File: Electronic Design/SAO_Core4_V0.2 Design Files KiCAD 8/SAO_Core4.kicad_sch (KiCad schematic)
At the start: 84 parts, among them Q1 MMBT4403LT1G, Q13 MMBT4403LT1G, Q14 MMBT4401LT1G, Q17 MMBT4403LT1G, Q18 MMBT4401LT1G, Q2 MMBT4401LT1G, Q21 Q_NMOS_DGS_AO3400A, Q22 SL3401A, Q3 MMBT4403LT1G, Q4 MMBT4401LT1G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

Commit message: Clean-up schematic DRC
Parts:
- removed X9: QWIIC, Connector_JST:JST_SH_SM04B-SRSS-TB_1x04-1MP_P1.00mm_Horizontal, symbol ANDY_SYMBOL_LIBRARY:Connector_QWIIC_4x1_MP
- added X3: QWIIC, Connector_JST:JST_SH_SM04B-SRSS-TB_1x04-1MP_P1.00mm_Horizontal, symbol ANDY_SYMBOL_LIBRARY:Connector_QWIIC_4x1_MP_P1.00
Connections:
- net GND: now also X3.1 (Pin_1)
- net SCL: now also X3.4 (Pin_4)
- net SDA: now also X3.3 (Pin_3)
- net at JP21.2 (C): now also X3.2 (Pin_2)
- net VMEM renamed 3V3

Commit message: Begin refinements for HWV0.2.0
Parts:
- removed JP21: V_SEL, Jumper:SolderJumper-3_P1.3mm_Bridged12_Pad1.0x1.5mm, symbol Jumper:SolderJumper_3_Bridged12
- removed JP22: INTA, Jumper:SolderJumper-2_P1.3mm_Open_Pad1.0x1.5mm, symbol Jumper:SolderJumper_2_Open
- removed JP23: INTB, Jumper:SolderJumper-2_P1.3mm_Open_Pad1.0x1.5mm, symbol Jumper:SolderJumper_2_Open
- removed JP24, JP25: CM_SNS_SEL, Jumper:SolderJumper-3_P1.3mm_Bridged12_Pad1.0x1.5mm, symbol Jumper:SolderJumper_3_Bridged12
- removed TP6: GPB6, Andy_Footprint_Library:TestPoint_THTPad_D1.5mm_Drill1.0mm, symbol Connector:TestPoint_Probe
- removed TP7: GPB7, Andy_Footprint_Library:TestPoint_THTPad_D1.5mm_Drill1.0mm, symbol Connector:TestPoint_Probe
- removed X2: SAO_conn_SFH11-NBPC-D03-ST-BK, Andy_Footprint_Library:Badgelife-SAOv169-BADGE-2x3, symbol ANDY_SYMBOL_LIBRARY:SAO_conn_SFH11-NBPC-D03-ST-BK-badgelife_shitty_addon_v169bis
- removed X3: QWIIC, Connector_JST:JST_SH_SM04B-SRSS-TB_1x04-1MP_P1.00mm_Horizontal, symbol ANDY_SYMBOL_LIBRARY:Connector_QWIIC_4x1_MP_P1.00
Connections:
- net GPIO2 is gone; now on net CM_SNS_PLS: X1.6 (GPIO2)
- net SPARE_GPA6 is gone; now on net CM_EN: U11.27 (GPA6)
- net CMDQ-7N9P renamed CMDQ-7N
- net CMDQ-7N: no longer R17.2
- net CMDQ-7P9N renamed CMDQ-7P
- net CMDQ-7P: no longer R18.2
- net SPARE_GPB6 renamed CMDQ-9N
- net CMDQ-9N: now also R18.2
- net SPARE_GPB7 renamed CMDQ-9P
- net CMDQ-9P: now also R17.2
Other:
- note added: "(SAO RX)"
- note added: "(SAO TX)"
- note added: "Learn about I2C GPIO Expanders here: https://learn.adafruit.com/adafruit-mcp23017-i2c-gpio-expander 7 Address bits: 010 0[A2-A1-A0] HEX 0x20 to 0x27 (default 27) DEC 32 to 39 (default 39)"
- note added: "SAO, I2C"
- note added: "Shift LED connections up 2 pins, tying B3/4 to 7N/7P. The order will look cleaner, and LED pixel numbering will match GPB numbers."
- note removed: "Learn about I2C GPIO Expanders here: https://learn.adafruit.com/adafruit-mcp23017-i2c-gpio-expander 7 Address bits: 010 0[A2-A1-A0] HEX 0x: 2 [0 to 7]"
- note removed: "QWIIC I2C"
- note removed: "SAO #2 (OUT/TOP)"
- note removed: "SAO, QWIIC, STEMMA QT, I2C"

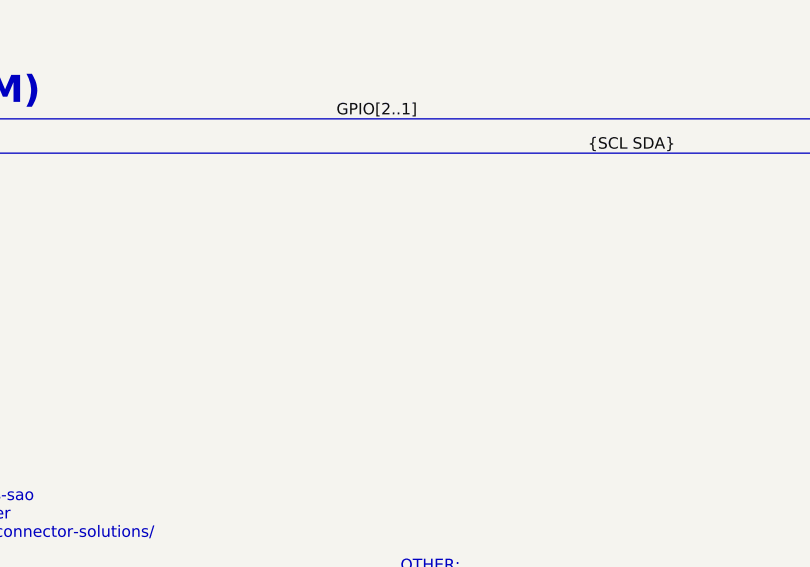
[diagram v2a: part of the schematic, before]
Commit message: Shrink V0.2 PCB size
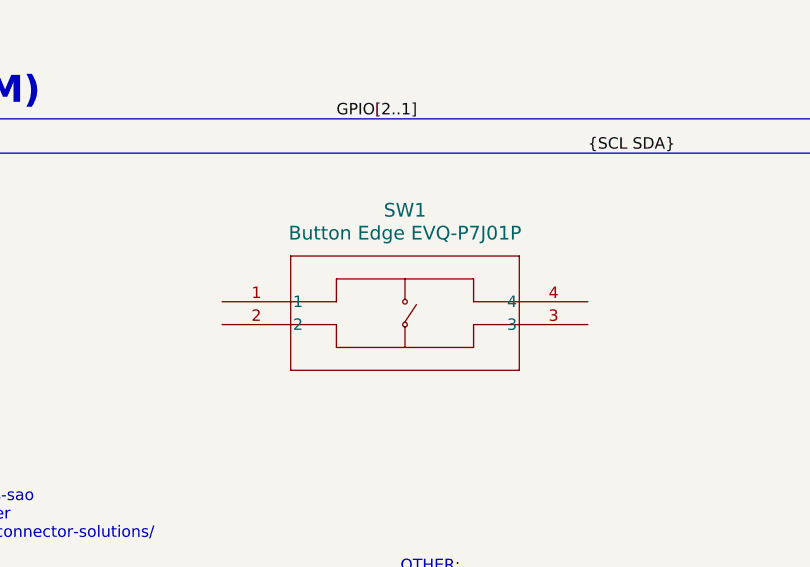
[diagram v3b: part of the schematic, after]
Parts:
- added SW1: Button Edge EVQ-P7J01P, SMD4_SW_EVQP7J_PAN, symbol ANDY_SYMBOL_LIBRARY:Button Edge EVQ-P7J01P
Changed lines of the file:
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@@
+	)
+	(symbol
+		(lib_id "ANDY_SYMBOL_LIBRARY:Button Edge EVQ-P7J01P")
+		(at 82.55 224.79 0)
+		(unit 1)
+		(exclude_from_sim no)
+		(in_bom yes)
+		(on_board yes)
+		(dnp no)
+		(fields_autoplaced yes)
+		(property "Reference" "SW1"
+			(at 102.87 214.63 0)
+			(effects
+				(font
+					(size 1.524 1.524)
+				)
+			)
+		)
+		(property "Value" "Button Edge EVQ-P7J01P"
+			(at 102.87 217.17 0)
+			(effects
+				(font
+					(size 1.524 1.524)
+				)
+			)
+		)
+		(property "Footprint" "SMD4_SW_EVQP7J_PAN"
+			(at 82.55 224.79 0)
+			(effects
+				(font
+					(size 1.27 1.27)
+					(italic yes)
+				)
+				(hide yes)
+			)
+		)
+		(property "Datasheet" "EVQ-P7J01P"
+			(at 82.55 224.79 0)
+			(effects
+				(font
+					(size 1.27 1.27)
+					(italic yes)
+				)
+				(hide yes)
+			)
+		)
+		(property "Description" ""
+			(at 82.55 224.79 0)
+			(effects
+				(font
+					(size 1.27 1.27)
+				)
+				(hide yes)
+			)
+		)
+		(pin "4"
+		)
+		(pin "3"
+		)
+		(pin "2"
+		)
+		(pin "1"
+		)
+		(instances
+			(project ""
+				(path "/4ac2dd59-cc2d-481f-806f-f2464072bc90"
+					(reference "SW1")
+					(unit 1)
+				)
+			)
+		)
 	)
 	(symbol

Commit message: HWV0.2: Create WIP schematics pdf and renders
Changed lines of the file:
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@@
 	(text "Shift LED connections up 2 pins, tying B3/4  to 7N/7P. \nThe order will look cleaner, and LED pixel numbering will match GPB numbers."
 		(exclude_from_sim no)
-		(at 302.514 215.392 0)
+		(at 306.578 293.37 0)
 		(effects
 			(font
